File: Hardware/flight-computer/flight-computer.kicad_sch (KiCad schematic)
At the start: 42 parts, among them J1 Conn_01x06_Pin, J2 Conn_01x06_Pin, J3 Power Connector, J4 Micro_SD_Card, J5 USB_C_Receptacle_USB2.0_16P, J6 Conn_01x02_Pin, Q1 DMN3404L, Q2 DMN3404L, U1 LMR51420X, U2 ESP32-S3-WROOM-1, U3 LSM6DSO32TR, U4 INA2180A1IDGKR

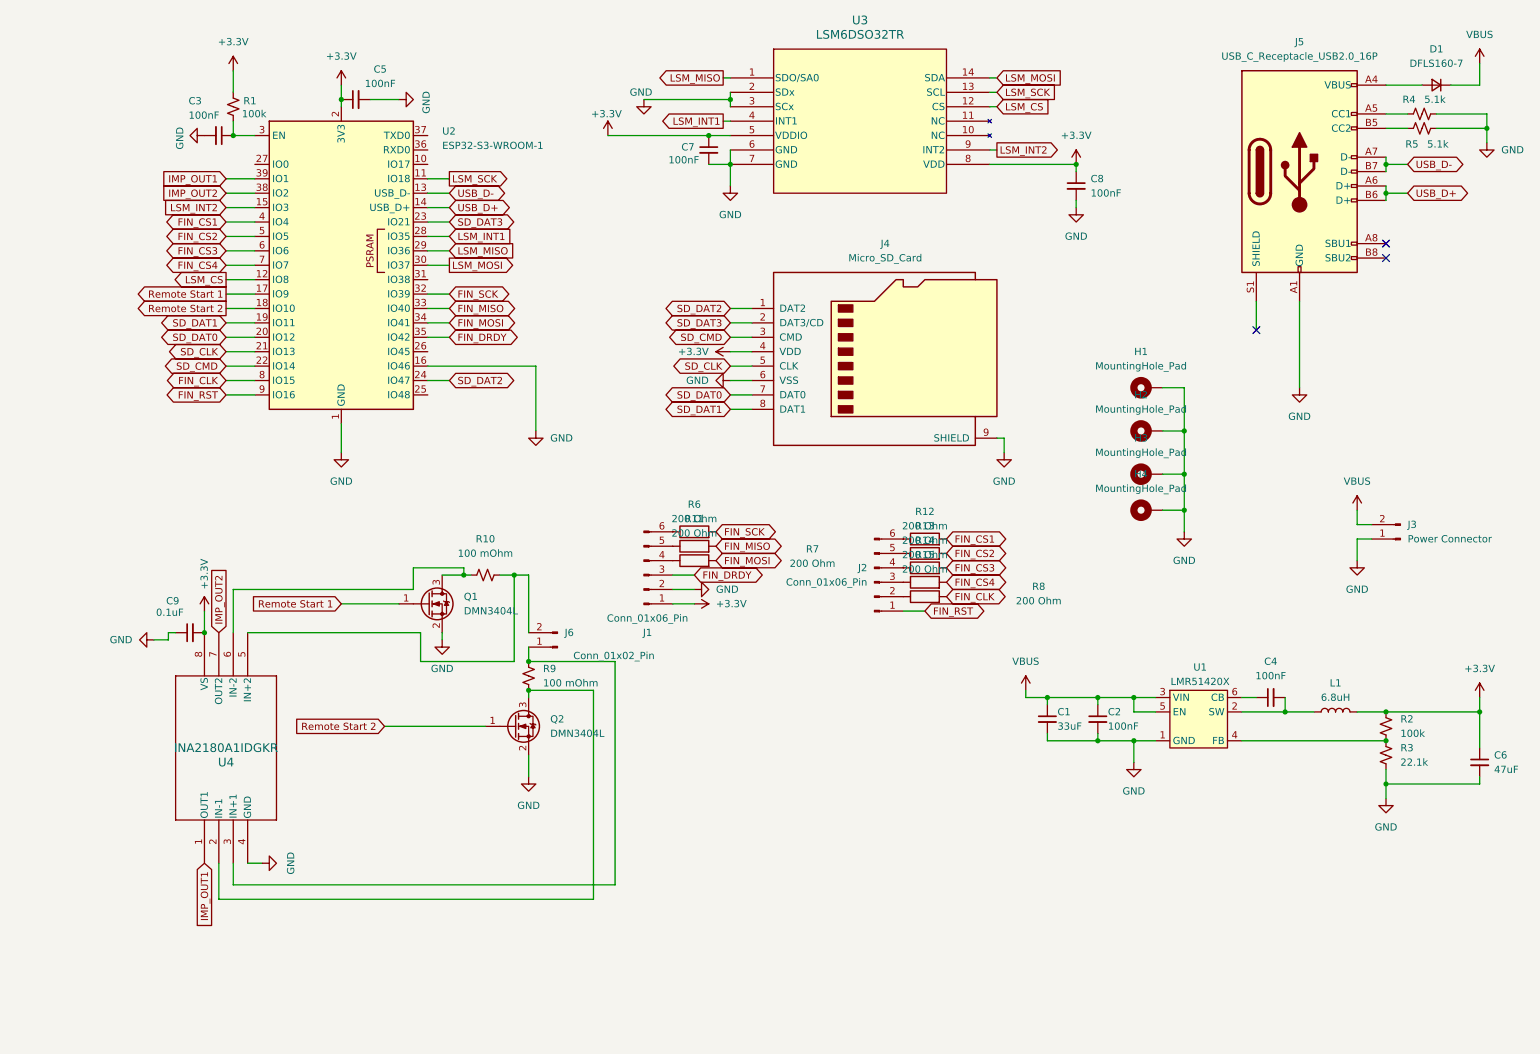
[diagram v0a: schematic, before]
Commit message: added barometer and 10p conn to esp
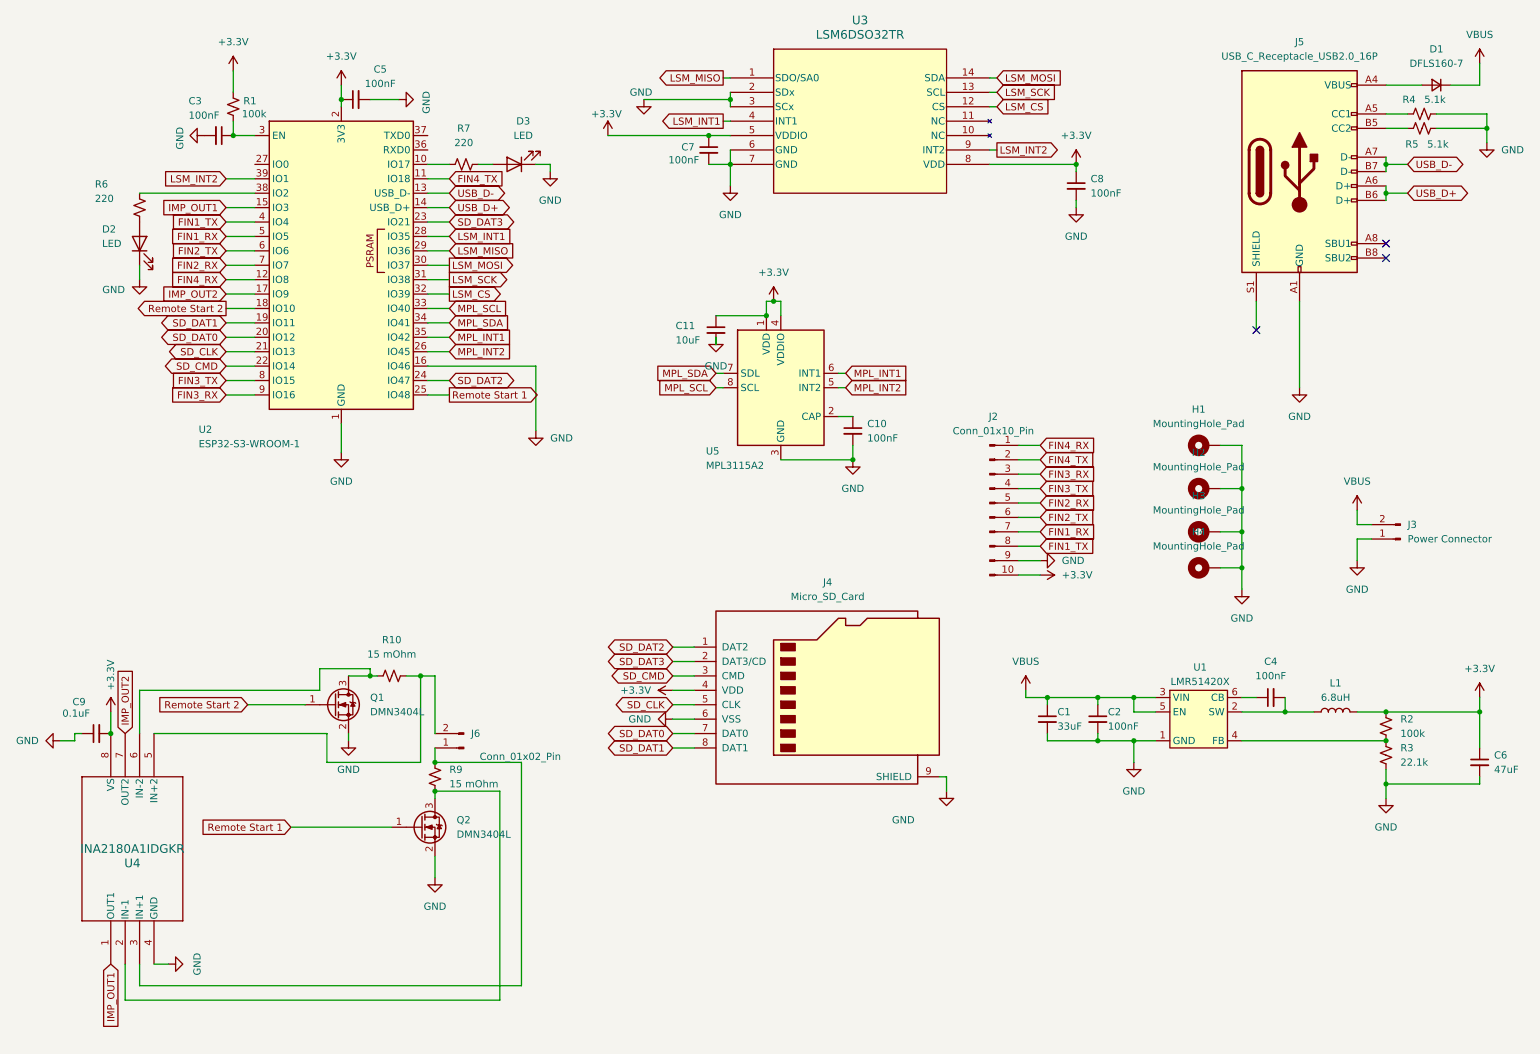
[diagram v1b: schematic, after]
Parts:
- removed J1, J2: Conn_01x06_Pin, Connector_JST:JST_ZE_SM06B-ZESS-TB_1x06-1MP_P1.50mm_Horizontal, symbol Connector:Conn_01x06_Pin
- removed R11, R12, R13, R14, R15, R6, R7, R8: 200 Ohm, Resistor_SMD:R_0402_1005Metric, symbol Device:R
- added C10: 100nF, Capacitor_SMD:C_0402_1005Metric, symbol Device:C_Small
- added C11: 10uF, Capacitor_SMD:C_0402_1005Metric, symbol Device:C_Small
- added D2, D3: LED, LED_SMD:LED_0603_1608Metric, symbol Device:LED
- added J2: Conn_01x10_Pin, Connector_JST:JST_ZE_SM10B-ZESS-TB_1x10-1MP_P1.50mm_Horizontal, symbol Connector:Conn_01x10_Pin
- added R6, R7: 220, Resistor_SMD:R_0402_1005Metric, symbol Device:R_Small_US
- added U5: MPL3115A2, Package_LGA:NXP_LGA-8_3x5mm_P1.25mm_H1.1mm, symbol Sensor_Pressure:MPL3115A2
- R10, R9: value 100 mOhm -> 15 mOhm
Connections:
- net FIN_SCK is gone; now on net LSM_CS: U2.32 (IO39)
- net +3.3V: now also C11.1, J2.10 (Pin_10), U5.1 (VDD), U5.4 (VDDIO)
- net GND: now also C10.2, C11.2, D2.1 (K), D3.1 (K), J2.9 (Pin_9), U5.3 (GND)
- net IMP_OUT1: now also U2.15 (IO3); no longer U2.39 (IO1)
- net IMP_OUT2: now also U2.17 (IO9); no longer U2.38 (IO2)
- net LSM_CS: no longer U2.12 (IO8)
- net LSM_INT2: now also U2.39 (IO1); no longer U2.15 (IO3)
- net LSM_SCK: now also U2.31 (IO38); no longer U2.11 (IO18)
- net Remote Start 1: now also Q2.1 (G), U2.25 (IO48); no longer Q1.1 (G), U2.17 (IO9)
- net Remote Start 2: now also Q1.1 (G); no longer Q2.1 (G)
- net at U2.10 (IO17): now also R7.1
- net MPL_INT2: now reaches U2.26 (IO45)
- net MPL_INT2: now also U5.5 (INT2)
- net FIN_CLK renamed FIN3_TX
- net FIN3_TX: now also J2.4 (Pin_4)
- net FIN_CS1 renamed FIN1_TX
- net FIN1_TX: now also J2.8 (Pin_8)
- net FIN_CS2 renamed FIN1_RX
- net FIN1_RX: now also J2.7 (Pin_7)
- net FIN_CS3 renamed FIN2_TX
- net FIN2_TX: now also J2.6 (Pin_6)
- net FIN_CS4 renamed FIN2_RX
- net FIN2_RX: now also J2.5 (Pin_5)
- net FIN_DRDY renamed MPL_INT1
- net MPL_INT1: now also U5.6 (INT1)
- net FIN_MISO renamed MPL_SCL
- net MPL_SCL: now also U5.8 (SCL)
- net FIN_MOSI renamed MPL_SDA
- net MPL_SDA: now also U5.7 (SDL)
- net FIN_RST renamed FIN3_RX
- net FIN3_RX: now also J2.3 (Pin_3)
- new net: D2.2 (A), R6.2
- new net: D3.2 (A), R7.2
- new net: C10.1, U5.2 (CAP)
- new net: R6.1, U2.38 (IO2)
- new net FIN4_RX: J2.1 (Pin_1), U2.12 (IO8)
- new net FIN4_TX: J2.2 (Pin_2), U2.11 (IO18)
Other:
- moved on the sheet: C9, H1, H2, H3, H4, J4, J6, Q1, Q2, R10, R9, U4

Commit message: finalish board
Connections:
- net +3.3V: now also D3.2 (A)
- net GND: no longer D3.1 (K)
- net at R7.1: now also U2.27 (IO0); no longer U2.10 (IO17)
- net at R7.2: now also D3.1 (K); no longer D3.2 (A)
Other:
- moved on the sheet: D3, R7
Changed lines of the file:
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@@
 	(wire
 		(pts
-			(xy 104.14 43.18) (xy 106.68 43.18)
+			(xy 36.83 43.18) (xy 34.29 43.18)
 		)
 		(stroke
@@
 	(wire
 		(pts
-			(xy 106.68 43.18) (xy 106.68 44.45)
+			(xy 34.29 43.18) (xy 34.29 41.91)
 		)
 		(stroke
@@
 	(wire
 		(pts
-			(xy 93.98 43.18) (xy 96.52 43.18)
+			(xy 46.99 43.18) (xy 44.45 43.18)
 		)
 		(stroke
@@
 	(wire
 		(pts
+			(xy 52.07 43.18) (xy 54.61 43.18)
+		)
+		(stroke
+			(width 0)
+			(type default)
+		)
+	)
+	(wire
+		(pts
 			(xy 85.09 55.88) (xy 88.9 55.88)
 		)
@@
 	(symbol
 		(lib_id "power:GND")
-		(at 106.68 44.45 0)
-		(unit 1)
-		(exclude_from_sim no)
-		(in_bom yes)
-		(on_board yes)
-		(dnp no)
-		(fields_autoplaced yes)
-		(property "Reference" "#PWR036"
-			(at 106.68 50.8 0)
-			(effects
-				(font
-					(size 1.27 1.27)
-				)
-				(hide yes)
-			)
-		)
-		(property "Value" "GND"
-			(at 106.68 49.53 0)
-			(effects
-				(font
-					(size 1.27 1.27)
-				)
-			)
-		)
-		(property "Footprint" ""
-			(at 106.68 44.45 0)
-			(effects
-				(font
-					(size 1.27 1.27)
-				)
-				(hide yes)
-			)
-		)
-		(property "Datasheet" ""
-			(at 106.68 44.45 0)
-			(effects
-				(font
-					(size 1.27 1.27)
-				)
-				(hide yes)
-			)
-		)
-		(property "Description" "Power symbol creates a global label with name \"GND\" , ground"
-			(at 106.68 44.45 0)
-			(effects
-				(font
-					(size 1.27 1.27)
-				)
-				(hide yes)
-			)
-		)
-		(pin "1"
-		)
-		(instances
-			(project ""
-				(path "/4ecd09a6-9393-48a2-99c4-3daa7c04326d"
-					(reference "#PWR036")
-					(unit 1)
-				)
-			)
-		)
-	)
-	(symbol
-		(lib_id "power:GND")
 		(at 20.32 144.78 270)
 		(unit 1)
@@
 		)
 		(property "Value" "GND"
-			(at 41.402 36.576 0)
+			(at 32.258 39.37 0)
 			(effects
 				(font
@@
 	(symbol
 		(lib_id "Device:R_Small_US")
-		(at 91.44 43.18 90)
+		(at 49.53 43.18 270)
 		(unit 1)
 		(exclude_from_sim no)
@@
 		(dnp no)
 		(property "Reference" "R7"
-			(at 91.44 36.83 90)
+			(at 49.53 49.53 90)
 			(effects
 				(font
@@
 		)
 		(property "Value" "220"
-			(at 91.44 39.37 90)
+			(at 49.53 46.99 90)
 			(effects
 				(font
@@
 		)
 		(property "Footprint" "Resistor_SMD:R_0402_1005Metric"
-			(at 98.044 33.274 0)
+			(at 42.926 53.086 0)
 			(effects
 				(font
@@
 		)
 		(property "Datasheet" "~"
-			(at 91.44 43.18 0)
+			(at 49.53 43.18 0)
 			(effects
 				(font
@@
 		)
 		(property "Description" "Resistor, small US symbol"
-			(at 91.44 43.18 0)
+			(at 49.53 43.18 0)
 			(effects
 				(font
@@
 	(symbol
 		(lib_id "Device:LED")
-		(at 100.33 43.18 180)
+		(at 40.64 43.18 180)
 		(unit 1)
 		(exclude_from_sim no)
@@
 		(fields_autoplaced yes)
 		(property "Reference" "D3"
-			(at 101.9175 35.56 0)
+			(at 42.2275 35.56 0)
 			(effects
 				(font
@@
 		)
 		(property "Value" "LED"
-			(at 101.9175 38.1 0)
+			(at 42.2275 38.1 0)
 			(effects
 				(font
@@
 		)
 		(property "Footprint" "LED_SMD:LED_0603_1608Metric"
-			(at 100.33 43.18 0)
+			(at 40.64 43.18 0)
 			(effects
 				(font
@@
 		)
 		(property "Datasheet" "~"
-			(at 100.33 43.18 0)
+			(at 40.64 43.18 0)
 			(effects
 				(font
@@
 		)
 		(property "Description" "Light emitting diode"
-			(at 100.33 43.18 0)
+			(at 40.64 43.18 0)
 			(effects
 				(font
@@
 		)
 		(property "Sim.Pins" "1=K 2=A"
-			(at 100.33 43.18 0)
+			(at 40.64 43.18 0)
 			(effects
 				(font
@@
 					(unit 1)
 				)
+			)
+		)
+	)
+	(symbol
+		(lib_id "power:+3.3V")
+		(at 34.29 41.91 0)
+		(unit 1)
+		(exclude_from_sim no)
+		(in_bom yes)
+		(on_board yes)
+		(dnp no)
+		(fields_autoplaced yes)
+		(property "Reference" "#PWR036"
+			(at 34.29 45.72 0)
+			(effects
+				(font
+					(size 1.27 1.27)
+				)
+				(hide yes)
+			)
+		)
+		(property "Value" "+3.3V"
+			(at 34.29 36.83 0)
+			(effects
+				(font
+					(size 1.27 1.27)
+				)
+			)
+		)
+		(property "Footprint" ""
+			(at 34.29 41.91 0)
+			(effects
+				(font
+					(size 1.27 1.27)
+				)
+				(hide yes)
+			)
+		)
+		(property "Datasheet" ""
+			(at 34.29 41.91 0)
+			(effects
+				(font
+					(size 1.27 1.27)
+				)
+				(hide yes)
+			)
+		)
+		(property "Description" "Power symbol creates a global label with name \"+3.3V\""
+			(at 34.29 41.91 0)
+			(effects
+				(font
+					(size 1.27 1.27)
+				)
+				(hide yes)
+			)
+		)
+		(pin "1"
+		)
+		(instances
+			(project ""
+				(path "/4ecd09a6-9393-48a2-99c4-3daa7c04326d"
+					(reference "#PWR036")
+					(unit 1)
+				)
